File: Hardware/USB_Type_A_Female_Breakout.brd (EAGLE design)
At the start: 20.3 x 25.4 mm, 12 parts

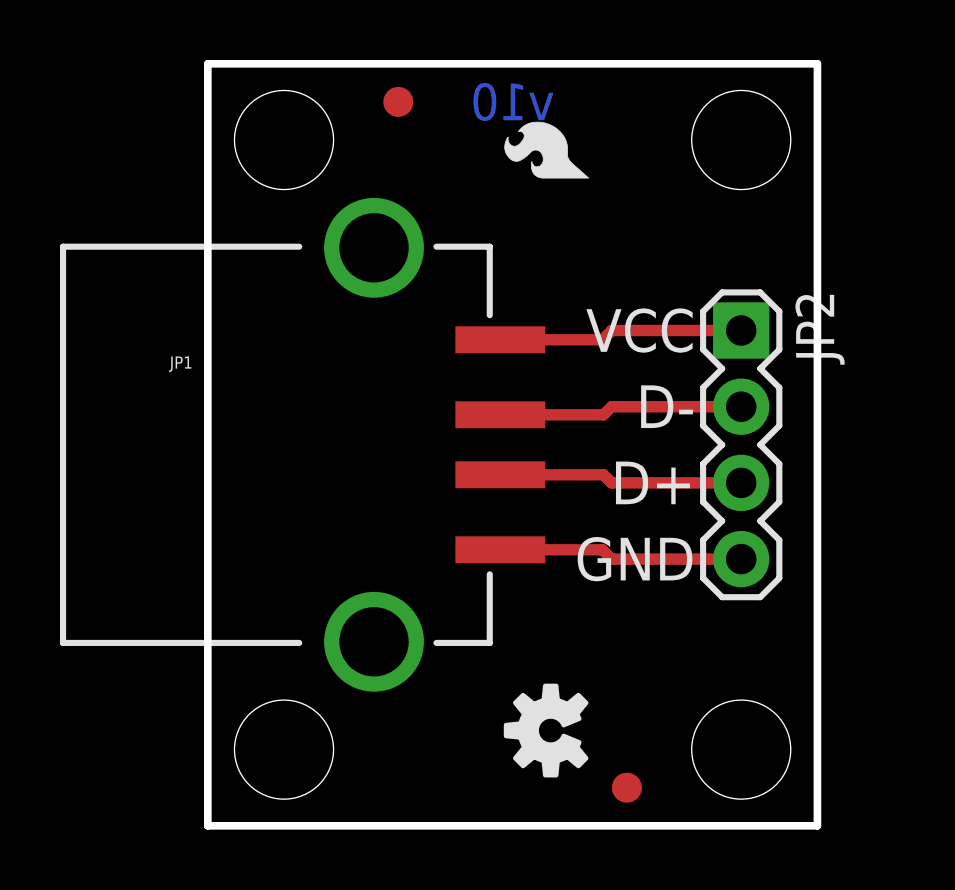
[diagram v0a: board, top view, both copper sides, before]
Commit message: Moved USB jack back. Added 0 Ohm DNP resistor to optionally connect USB jack shield to GND.
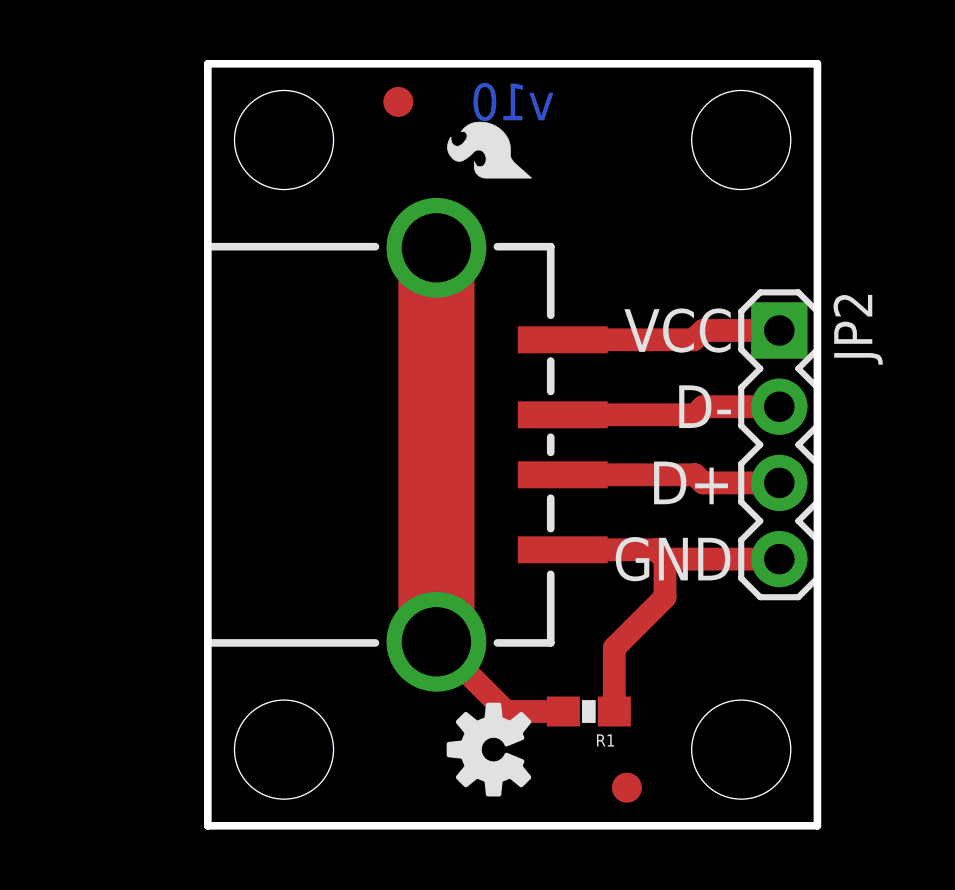
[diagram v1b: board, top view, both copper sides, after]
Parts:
- added R1: 0, SparkFun-Resistors:0603-RES
- JP1: value USB_ -> USB+SHIELDUSB-A-S-NOSILK-FEMALE; device SparkFun-Connectors:USB-A-S-SILK-FEMALE -> SparkFun-Connectors:USB-A-S-NOSILK-FEMALE
- moved JP1 5.08 mm to (7.62, 12.7)
- moved LOGO2 2.01 mm to (9.53, 2.54)
- moved LOGO3 1.90 mm to (10.8, 21.6)
- moved JP2 1.27 mm to (19.1, 16.5)
- moved LOGO1 1.27 mm to (12.7, 21.8)
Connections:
- new net N$1: JP1.S1, JP1.S2, R1.2
- net GND: now also R1.1
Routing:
- net N$1: track 0.00 -> 18.3 mm
- net GND: track 8.16 -> 13.1 mm
- net VCC: track 8.16 -> 7.35 mm
- net D-: track 8.14 -> 7.33 mm
- net D+: track 8.14 -> 7.33 mm

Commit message: Add Board Dimensions
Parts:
- moved FRAME1 2.54 mm to (-15.2, -20.3)
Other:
- board text added: "Dimensions in inches."
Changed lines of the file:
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@@
 <?xml version="1.0" encoding="utf-8"?>
 <!DOCTYPE eagle SYSTEM "eagle.dtd">
-<eagle version="6.5.0">
+<eagle version="9.4.2">
 <drawing>
 <settings>
-<setting alwaysvectorfont="yes"/>
+<setting alwaysvectorfont="no"/>
+<setting keepoldvectorfont="yes"/>
 <setting verticaltext="up"/>
 </settings>
@@
 <layer number="37" name="tTest" color="7" fill="1" visible="no" active="no"/>
 <layer number="38" name="bTest" color="7" fill="1" visible="no" active="no"/>
-<layer number="47" name="Measures" color="7" fill="1" visible="no" active="no"/>
+<layer number="47" name="Measures" color="7" fill="1" visible="no" active="yes"/>
 <layer number="48" name="Document" color="7" fill="1" visible="no" active="no"/>
 <layer number="49" name="Reference" color="7" fill="1" visible="no" active="no"/>
@@
 <text x="2.54" y="12.7" size="1.016" layer="22" font="vector" ratio="15" rot="SMR270" align="bottom-center">USB Type A Female</text>
 <text x="4.318" y="12.7" size="1.016" layer="22" font="vector" ratio="15" rot="SMR270" align="bottom-center">Breakout</text>
-<text x="15.24" y="-17.78" size="1.778" layer="51" font="vector" ratio="15">Shawn Hymel</text>
+<text x="15.24" y="-20.32" size="1.778" layer="51" font="vector" ratio="15">Shawn Hymel</text>
 <text x="10.16" y="24.13" size="1.2192" layer="16" font="vector" ratio="15" rot="MR0" align="center">v10</text>
 <wire x1="0" y1="19.304" x2="5.588" y2="19.304" width="0.254" layer="21"/>
@@
 <wire x1="11.43" y1="8.382" x2="11.43" y2="6.096" width="0.254" layer="21"/>
 <wire x1="11.43" y1="6.096" x2="9.652" y2="6.096" width="0.254" layer="21"/>
+<dimension x1="0" y1="0" x2="20.32" y2="0" x3="10.16" y3="-3.81" textsize="1.778" textratio="15" layer="47" unit="inch"/>
+<dimension x1="20.32" y1="0" x2="20.32" y2="2.54" x3="24.13" y3="1.27" textsize="1.778" textratio="15" layer="47" unit="inch"/>
+<dimension x1="20.32" y1="0" x2="17.78" y2="0" x3="19.05" y3="-7.62" textsize="1.778" textratio="15" layer="47" unit="inch"/>
+<dimension x1="20.32" y1="0" x2="20.32" y2="12.7" x3="31.75" y3="6.35" textsize="1.778" textratio="15" layer="47" unit="inch"/>
+<dimension x1="0" y1="0" x2="0" y2="12.7" x3="-3.81" y3="6.35" textsize="1.778" textratio="15" layer="47" unit="inch"/>
+<text x="-7.62" y="-12.7" size="1.778" layer="47" font="vector" ratio="15">Dimensions in inches.</text>
+<dimension x1="2.54" y1="2.54" x2="2.54" y2="22.86" x3="-7.62" y3="12.7" textsize="1.778" textratio="15" layer="47" unit="inch"/>
+<dimension x1="0" y1="0" x2="0" y2="25.4" x3="-11.43" y3="12.7" textsize="1.778" textratio="15" layer="47" unit="inch"/>
+<dimension x1="17.78" y1="22.86" x2="17.78" y2="25.4" x3="24.13" y3="24.13" textsize="1.778" textratio="15" layer="47" unit="inch"/>
+<dimension x1="20.32" y1="25.4" x2="17.78" y2="22.86" x3="19.05" y3="34.29" textsize="1.778" textratio="15" layer="47" dtype="horizontal" unit="inch"/>
+<dimension x1="17.78" y1="22.86" x2="2.54" y2="22.86" x3="10.16" y3="36.83" textsize="1.778" textratio="15" layer="47" dtype="horizontal" unit="inch"/>
 </plain>
 <attributes>
@@
 <param name="dpMaxLengthDifference" value="10mm"/>
 <param name="dpGapFactor" value="2.5"/>
-<param name="checkGrid" value="0"/>
 <param name="checkAngle" value="0"/>
 <param name="checkFont" value="1"/>
 <param name="checkRestrict" value="1"/>
+<param name="checkStop" value="0"/>
+<param name="checkValues" value="0"/>
+<param name="checkNames" value="1"/>
+<param name="checkWireStubs" value="1"/>
+<param name="checkPolygonWidth" value="0"/>
 <param name="useDiameter" value="13"/>
 <param name="maxErrors" value="50"/>
@@
 <pass name="Default">
 <param name="RoutingGrid" value="50mil"/>
+<param name="AutoGrid" value="1"/>
+<param name="Efforts" value="0"/>
+<param name="TopRouterVariant" value="1"/>
 <param name="tpViaShape" value="round"/>
 <param name="PrefDir.1" value="|"/>
@@
 </autorouter>
 <elements>
-<element name="FRAME1" library="SparkFun-Aesthetics" package="CREATIVE_COMMONS" value="FRAME-LETTER" x="-15.24" y="-17.78"/>
-<element name="JP1" library="SparkFun-Connectors" package="USB-A-S-NOSILK-FEMALE" value="USB+SHIELDUSB-A-S-NOSILK-FEMALE" x="7.62" y="12.7"/>
-<element name="JP2" library="SparkFun-Connectors" package="1X04" value="" x="19.05" y="16.51" rot="R270"/>
-<element name="STANDOFF1" library="SparkFun-Electromechanical" package="STAND-OFF" value="STAND-OFF" x="2.54" y="22.86"/>
-<element name="STANDOFF2" library="SparkFun-Electromechanical" package="STAND-OFF" value="STAND-OFF" x="2.54" y="2.54"/>
-<element name="STANDOFF3" library="SparkFun-Electromechanical" package="STAND-OFF" value="STAND-OFF" x="17.78" y="22.86"/>
-<element name="STANDOFF4" library="SparkFun-Electromechanical" package="STAND-OFF" value="STAND-OFF" x="17.78" y="2.54"/>
-<element name="LOGO1" library="SparkFun-Aesthetics" package="SFE-NEW-WEBLOGO" value="LOGO-SFENEW" x="12.7" y="21.844" rot="MR270"/>
-<element name="FID1" library="SparkFun-Aesthetics" package="FIDUCIAL-1X2" value="FIDUCIAL1X2" x="13.97" y="1.27"/>
-<element name="FID2" library="SparkFun-Aesthetics" package="FIDUCIAL-1X2" value="FIDUCIAL1X2" x="6.35" y="24.13"/>
-<element name="LOGO2" library="SparkFun-Aesthetics" package="OSHW-LOGO-S" value="OSHW-LOGOS" x="9.525" y="2.54" rot="R90"/>
-<element name="LOGO3" library="SparkFun-Aesthetics" package="SFE-LOGO-FLAME" value="LOGO-SFESK" x="10.795" y="21.59" rot="R90"/>
-<element name="R1" library="SparkFun-Resistors" package="0603-RES" value="0" x="12.7" y="3.81" rot="R180">
+<element name="FRAME1" library="SparkFun-Aesthetics" package="CREATIVE_COMMONS" value="FRAME-LETTER" x="-15.24" y="-20.32" smashed="yes"/>
+<element name="JP1" library="SparkFun-Connectors" package="USB-A-S-NOSILK-FEMALE" value="USB+SHIELDUSB-A-S-NOSILK-FEMALE" x="7.62" y="12.7" smashed="yes">
+<attribute name="NAME" x="16.08" y="5.495" size="1.27" layer="51" rot="R180"/>
+</element>
+<element name="JP2" library="SparkFun-Connectors" package="1X04" value="" x="19.05" y="16.51" smashed="yes" rot="R270">
+<attribute name="NAME" x="20.8788" y="17.8562" size="1.27" layer="25" ratio="10" rot="R270"/>
+<attribute name="VALUE" x="15.875" y="17.78" size="1.27" layer="27" rot="R270"/>
+</element>
+<element name="STANDOFF1" library="SparkFun-Electromechanical" package="STAND-OFF" value="STAND-OFF" x="2.54" y="22.86" smashed="yes"/>
+<element name="STANDOFF2" library="SparkFun-Electromechanical" package="STAND-OFF" value="STAND-OFF" x="2.54" y="2.54" smashed="yes"/>
+<element name="STANDOFF3" library="SparkFun-Electromechanical" package="STAND-OFF" value="STAND-OFF" x="17.78" y="22.86" smashed="yes"/>
+<element name="STANDOFF4" library="SparkFun-Electromechanical" package="STAND-OFF" value="STAND-OFF" x="17.78" y="2.54" smashed="yes"/>
+<element name="LOGO1" library="SparkFun-Aesthetics" package="SFE-NEW-WEBLOGO" value="LOGO-SFENEW" x="12.7" y="21.844" smashed="yes" rot="MR270"/>
+<element name="FID1" library="SparkFun-Aesthetics" package="FIDUCIAL-1X2" value="FIDUCIAL1X2" x="13.97" y="1.27" smashed="yes"/>
+<element name="FID2" library="SparkFun-Aesthetics" package="FIDUCIAL-1X2" value="FIDUCIAL1X2" x="6.35" y="24.13" smashed="yes"/>
+<element name="LOGO2" library="SparkFun-Aesthetics" package="OSHW-LOGO-S" value="OSHW-LOGOS" x="9.525" y="2.54" smashed="yes" rot="R90"/>
+<element name="LOGO3" library="SparkFun-Aesthetics" package="SFE-LOGO-FLAME" value="LOGO-SFESK" x="10.795" y="21.59" smashed="yes" rot="R90"/>
+<element name="R1" library="SparkFun-Resistors" package="0603-RES" value="0" x="12.7" y="3.81" smashed="yes" rot="R180">
+<attribute name="NAME" x="13.589" y="3.048" size="0.4064" layer="25" font="vector" rot="R180"/>
 <attribute name="PLACE" value="DNP" x="12.7" y="3.81" size="1.778" layer="27" rot="R180" display="off"/>
+<attribute name="VALUE" x="13.716" y="4.953" size="0.4064" layer="27" font="vector" rot="R180"/>
 </element>
 </elements>
@@
 </signal>
 </signals>
+<mfgpreviewcolors>
+<mfgpreviewcolor name="soldermaskcolor" color="0xC8008000"/>
+<mfgpreviewcolor name="silkscreencolor" color="0xFFFEFEFE"/>
+<mfgpreviewcolor name="backgroundcolor" color="0xFF282828"/>
+<mfgpreviewcolor name="coppercolor" color="0xFFFFBF00"/>
+<mfgpreviewcolor name="substratecolor" color="0xFF786E46"/>
+</mfgpreviewcolors>
 </board>
 </drawing>
